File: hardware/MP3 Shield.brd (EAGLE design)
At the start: 53.3 x 59.7 mm, 71 parts, among them Q1 12.288MHz, U1 3.3V, U2 ARDUINO_R3_SHIELD, U3 VS1053, U4 1.8V, U6 USD-SOCKET, U7 74HC4050 LVL CONVERTER

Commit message: Final touches to layout
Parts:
- moved FRAME2 70.3 mm to (-19.1, -11.4)
- moved U$5 11.4 mm to (50.8, 6.35)
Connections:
- net 3.3V: no longer R5.1
- net GND: now also R5.1
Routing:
- net 3.3V: track 168.5 -> 166.7 mm, vias 9 -> 8
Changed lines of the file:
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@@
 <element name="U4" library="SparkFun" package="SC70" value="1.8V" x="43.18" y="40.64" rot="R90"/>
 <element name="U$4" library="SparkFun" package="FIDUCIAL-1X2" value="FIDUCIAL1X2" x="7.62" y="54.61"/>
-<element name="U$5" library="SparkFun" package="FIDUCIAL-1X2" value="FIDUCIAL1X2" x="62.23" y="6.35"/>
+<element name="U$5" library="SparkFun" package="FIDUCIAL-1X2" value="FIDUCIAL1X2" x="50.8" y="6.35"/>
 <element name="U$8" library="SparkFun" package="SFE-NEW-WEBLOGO" value="LOGO-SFENEW" x="36.068" y="52.451" rot="MR0"/>
 <element name="S2" library="SparkFun" package="TACTILE_SWITCH_SMD" value="Reset" x="49.53" y="12.7" rot="R90"/>
@@
 <element name="R23" library="SparkFun" package="0603-RES" value="1K" x="41.91" y="26.67"/>
 <element name="R24" library="SparkFun" package="0603-RES" value="100K" x="40.64" y="24.13" rot="R90"/>
-<element name="FRAME2" library="SparkFun-Aesthetics" package="CREATIVE_COMMONS" value="FRAME-LETTER" x="-43.18" y="-77.47"/>
+<element name="FRAME2" library="SparkFun-Aesthetics" package="CREATIVE_COMMONS" value="FRAME-LETTER" x="-19.05" y="-11.43"/>
 </elements>
 <signals>
@@
 <via x="21.59" y="25.4" extent="1-16" drill="0.508"/>
 <via x="19.05" y="30.48" extent="1-16" drill="0.508"/>
+<contactref element="R5" pad="1"/>
 </signal>
 <signal name="VCC">
@@
 <contactref element="U4" pad="3"/>
 <contactref element="TP1" pad="P$1"/>
-<contactref element="R5" pad="1"/>
 <contactref element="U6" pad="4"/>
 <contactref element="U7" pad="1"/>
@@
 <wire x1="40.64" y1="51.562" x2="41.148" y2="52.07" width="0.254" layer="1"/>
 <wire x1="41.148" y1="52.07" x2="42.33" y2="52.07" width="0.254" layer="1"/>
-<wire x1="29.21" y1="43.561" x2="29.21" y2="44.87" width="0.254" layer="1"/>
-<wire x1="29.591" y1="43.18" x2="29.21" y2="43.561" width="0.254" layer="1"/>
-<wire x1="29.5" y1="43.18" x2="30.48" y2="43.18" width="0.254" layer="16"/>
-<wire x1="25.4" y1="39.08" x2="29.5" y2="43.18" width="0.254" layer="16"/>
-<wire x1="30.48" y1="43.18" x2="29.591" y2="43.18" width="0.254" layer="1"/>
 <via x="40.64" y="45.72" extent="1-16" drill="0.508"/>
-<via x="30.48" y="43.18" extent="1-16" drill="0.508"/>
 <via x="25.4" y="39.08" extent="1-16" drill="0.508"/>
 <via x="7.62" y="25.4" extent="1-16" drill="0.508"/>
@@
 <wire x1="41.78" y1="43.18" x2="41.78" y2="44.32" width="0.254" layer="1"/>
 <wire x1="40.701" y1="47.31" x2="40.64" y2="47.371" width="0.254" layer="1"/>
-<wire x1="40.64" y1="45.72" x2="31.75" y2="45.72" width="0.254" layer="16"/>
-<wire x1="31.75" y1="45.72" x2="30.48" y2="44.45" width="0.254" layer="16"/>
-<wire x1="30.48" y1="44.45" x2="30.48" y2="43.18" width="0.254" layer="16"/>
+<wire x1="40.64" y1="45.72" x2="29.21" y2="45.72" width="0.254" layer="16"/>
 <via x="41.91" y="31.75" extent="1-16" drill="0.508"/>
 <wire x1="41.91" y1="31.75" x2="41.91" y2="22.86" width="0.254" layer="16"/>
@@
 <wire x1="33.02" y1="30.861" x2="41.021" y2="30.861" width="0.254" layer="1"/>
 <wire x1="41.021" y1="30.861" x2="41.91" y2="31.75" width="0.254" layer="1"/>
+<wire x1="25.4" y1="39.08" x2="25.4" y2="41.91" width="0.254" layer="16"/>
+<wire x1="25.4" y1="41.91" x2="29.21" y2="45.72" width="0.254" layer="16"/>
 </signal>
 <signal name="1.8V">
@@
 </signal>
 </signals>
-<errors>
-</errors>
 </board>
 </drawing>

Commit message: Adding transistor part #s
Commits at 32,000 ft! Whooo!
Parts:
- Q2, Q3: value (none) -> PMBT3906
- Q4, Q5: value (none) -> MMBT2222
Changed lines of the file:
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@@
 <element name="C19" library="SparkFun" package="0603-CAP" value="3.3nF" x="38.1" y="15.24"/>
 <element name="C20" library="SparkFun" package="0603-CAP" value="3.3nF" x="38.1" y="25.4"/>
-<element name="Q2" library="SparkFun-DiscreteSemi" package="SOT23-3" value="" x="41.91" y="20.32" rot="R180"/>
-<element name="Q3" library="SparkFun-DiscreteSemi" package="SOT23-3" value="" x="41.91" y="10.16" rot="R180"/>
-<element name="Q4" library="SparkFun-DiscreteSemi" package="SOT23-3" value="" x="38.1" y="19.05" rot="R90"/>
-<element name="Q5" library="SparkFun-DiscreteSemi" package="SOT23-3" value="" x="38.1" y="8.89" rot="R90"/>
+<element name="Q2" library="SparkFun-DiscreteSemi" package="SOT23-3" value="PMBT3906" x="41.91" y="20.32" rot="R180"/>
+<element name="Q3" library="SparkFun-DiscreteSemi" package="SOT23-3" value="PMBT3906" x="41.91" y="10.16" rot="R180"/>
+<element name="Q4" library="SparkFun-DiscreteSemi" package="SOT23-3" value="MMBT2222" x="38.1" y="19.05" rot="R90"/>
+<element name="Q5" library="SparkFun-DiscreteSemi" package="SOT23-3" value="MMBT2222" x="38.1" y="8.89" rot="R90"/>
 <element name="SJ4" library="SparkFun" package="SJ_2S-TRACE" value="NC" x="41.91" y="29.21" rot="R180"/>
 <element name="R23" library="SparkFun" package="0603-RES" value="1K" x="41.91" y="26.67"/>

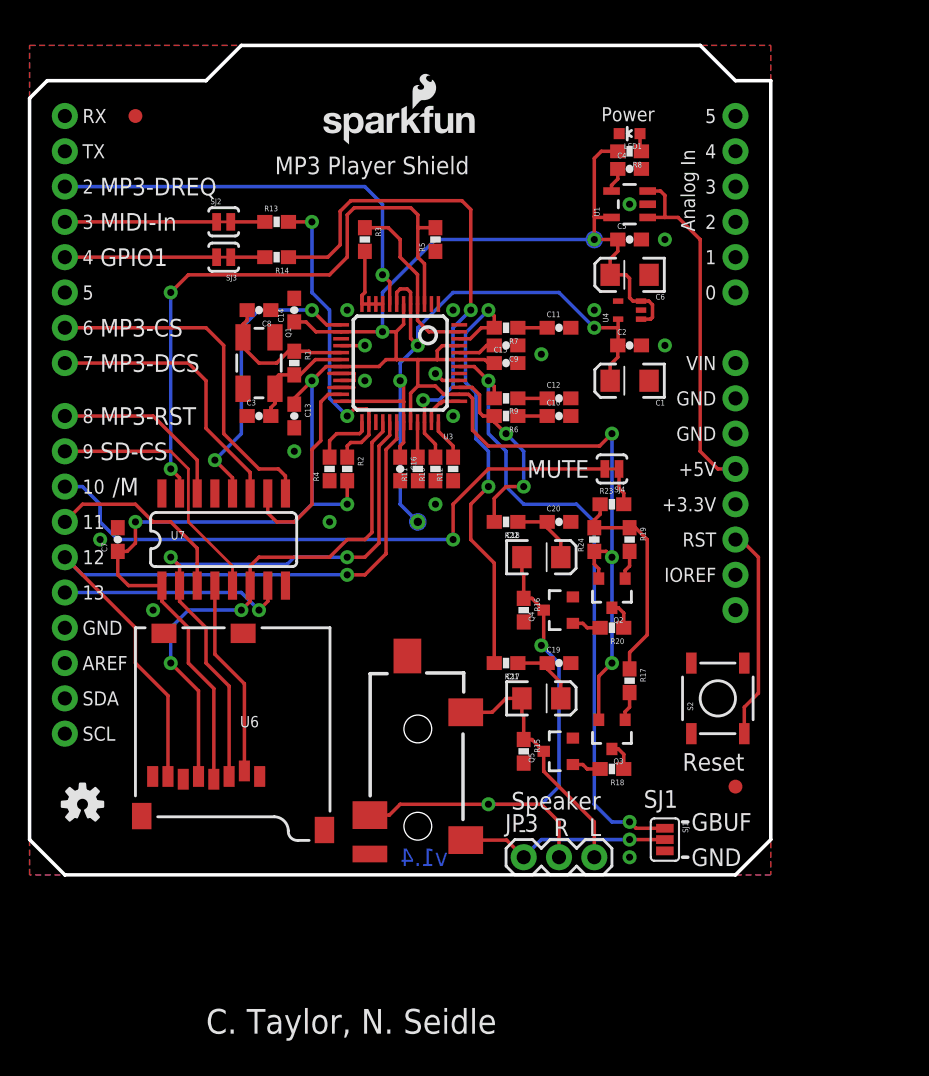
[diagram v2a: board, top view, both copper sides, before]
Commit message: Added ISP connector for compatibility with Lenoardo/Mega.
Routed SPI pins to ISP connector for more compatibility between Arduino
versions.
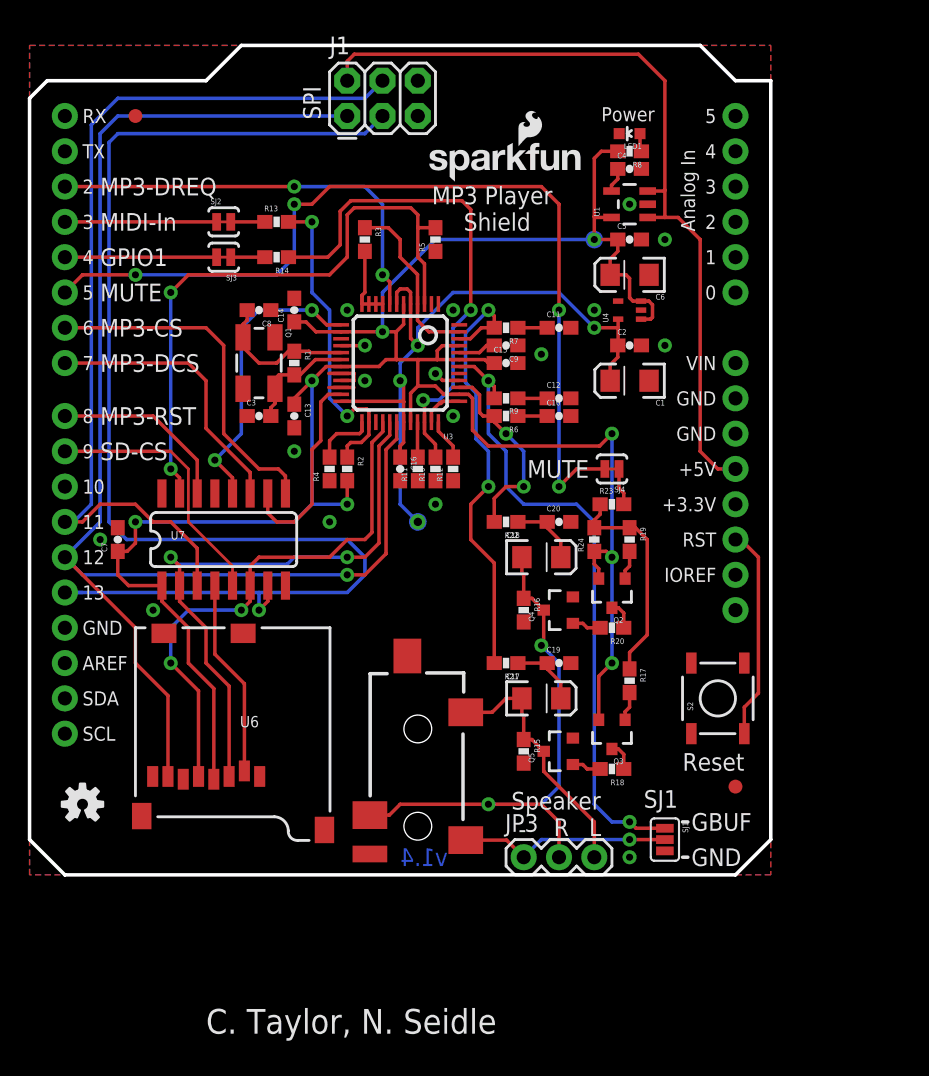
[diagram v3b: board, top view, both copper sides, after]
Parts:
- removed FRAME2: FRAME-LETTER, SparkFun-Aesthetics:CREATIVE_COMMONS
- added FRAME1: FRAME-LEDGER, SparkFun-Aesthetics:CREATIVE_COMMONS
- added J1: ISP/SPI, SparkFun:2X3
- moved LOGO2 8.07 mm to (28.3, 49.8)
- moved U$8 6.35 mm to (36.1, 46.1)
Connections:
- removed net N$13: SJ4.2, U2.D10
- new net 5V-MUTE: SJ4.2, U2.D5
- net 5V-MOSI: now also J1.4
- net 5V-SCK: now also J1.3
- net GND: now also J1.6
- net MISO: now also J1.1
- net VCC: now also J1.2
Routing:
- net 5V-SCK: track 16.5 -> 95.2 mm
- net 5V-MUTE: track 0.00 -> 65.6 mm, vias 0 -> 4
- net 5V-MOSI: track 14.0 -> 66.1 mm
- net MISO: track 52.9 -> 102.7 mm
- net N$13: track 44.8 -> 0.00 mm, vias 1 -> 0
- net VCC: track 25.7 -> 59.1 mm
- net MP3-DREQ: vias 1 -> 2
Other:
- board text added: "MP3 Player"
- board text added: "SPI"
- board text added: "Shield"
- board text removed: "/M"

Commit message: Updated 3.5mm jack and HEX inverter footprints.
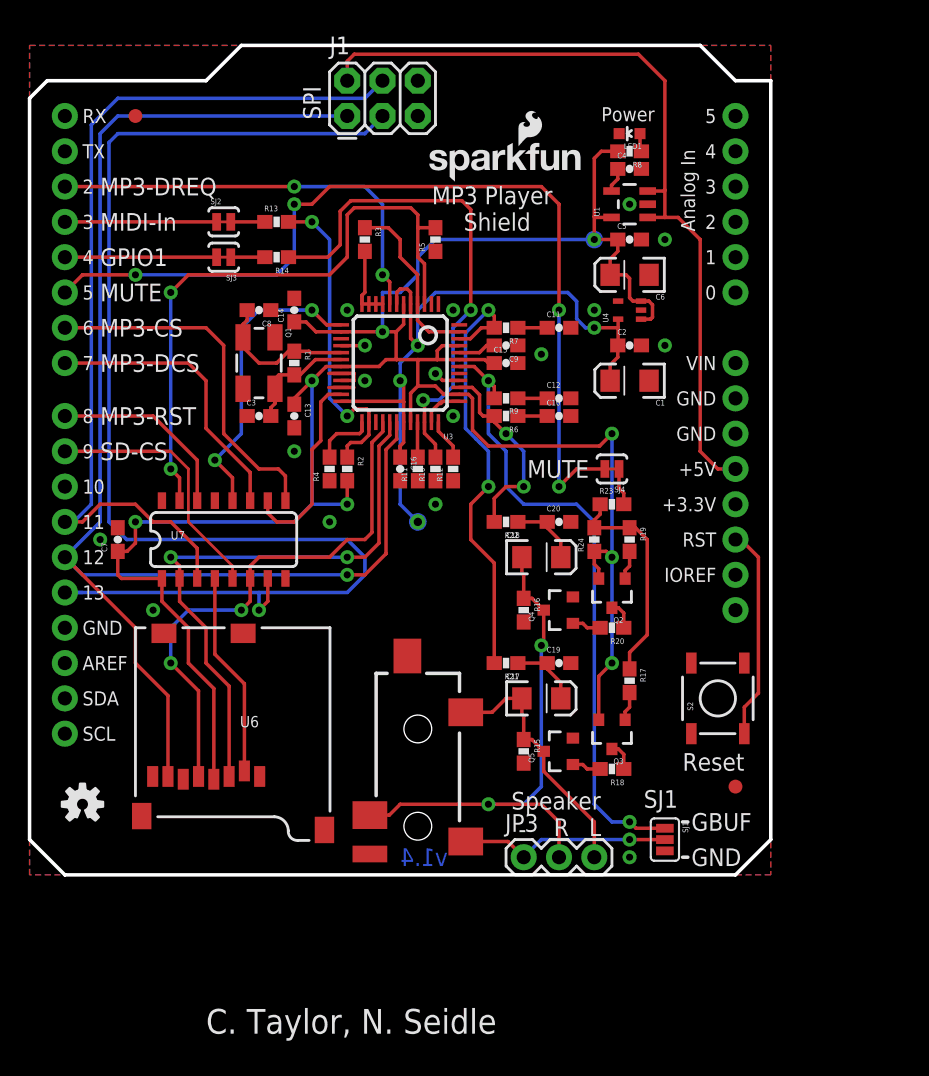
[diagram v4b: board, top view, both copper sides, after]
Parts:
- C1, C17, C18, C6: device SparkFun:EIA3216 -> SparkFun-Capacitors:EIA3216
- C10, C11, C12, C13, C14, C15, C16, C19, C2, C20, C3, C4, C5, C7, C8, C9: device SparkFun:0603-CAP -> SparkFun-Capacitors:0603-CAP
- JP1: device SparkFun:AUDIO-JACK-3.5MM-SMD -> SparkFun-Connectors:AUDIO-JACK-3.5MM-SMD
- LED1: device SparkFun:LED-0603 -> SparkFun-LED:LED-0603
- Q4, Q5: value MMBT2222 -> MMBT2222A
- R1, R10, R11, R12, R13, R14, R15, R16, R17, R18, R19, R2, R20, R21, R22, R23, R24, R3, R4, R5, R6, R7, R8, R9: device SparkFun:0603-RES -> SparkFun-Resistors:0603-RES
- S2: device SparkFun:TACTILE_SWITCH_SMD -> SparkFun-Electromechanical:TACTILE_SWITCH_SMD
- U1: device SparkFun:SOT23-5 -> SparkFun-PowerIC:SOT23-5
- U3: device SparkFun:LQFP-48 -> SparkFun-DigitalIC:LQFP-48
- U4: device SparkFun:SC70 -> SparkFun-PowerIC:SC70
- U7: device SparkFun:SO016 -> SparkFun-DigitalIC:SO016
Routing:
- net SPKR-R: track 40.7 -> 38.9 mm
- net 1.8V: track 52.5 -> 54.0 mm
- net 3.3V: track 166.7 -> 167.8 mm
- net MP3-DCS: track 21.4 -> 21.9 mm
- net MP3-CS: track 14.7 -> 14.2 mm
- net 5V-MP3-RST: track 13.2 -> 13.8 mm
- net 5V-MP3-DCS: track 20.1 -> 20.6 mm
- net 5V-MP3-CS: track 25.3 -> 25.8 mm
- net SD-CS: track 14.2 -> 14.7 mm
- net MP3-RST: track 44.9 -> 45.4 mm
- net 5V-SD-CS: track 19.1 -> 18.6 mm
- net 5V-SCK: track 95.2 -> 95.7 mm
- net 5V-MOSI: track 66.1 -> 65.5 mm
